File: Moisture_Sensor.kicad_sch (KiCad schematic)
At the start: 17 parts, among them J1 UPDI, J2 OLED SSD1306 0.96in, J3 SOIL SENSOR v1.2, J5 BATTERY 3xAAA, Q1 DMG3415U, SW1 READ BUTTON, U1 ATtiny1614-SSNR, U2 TPS22917DBVR

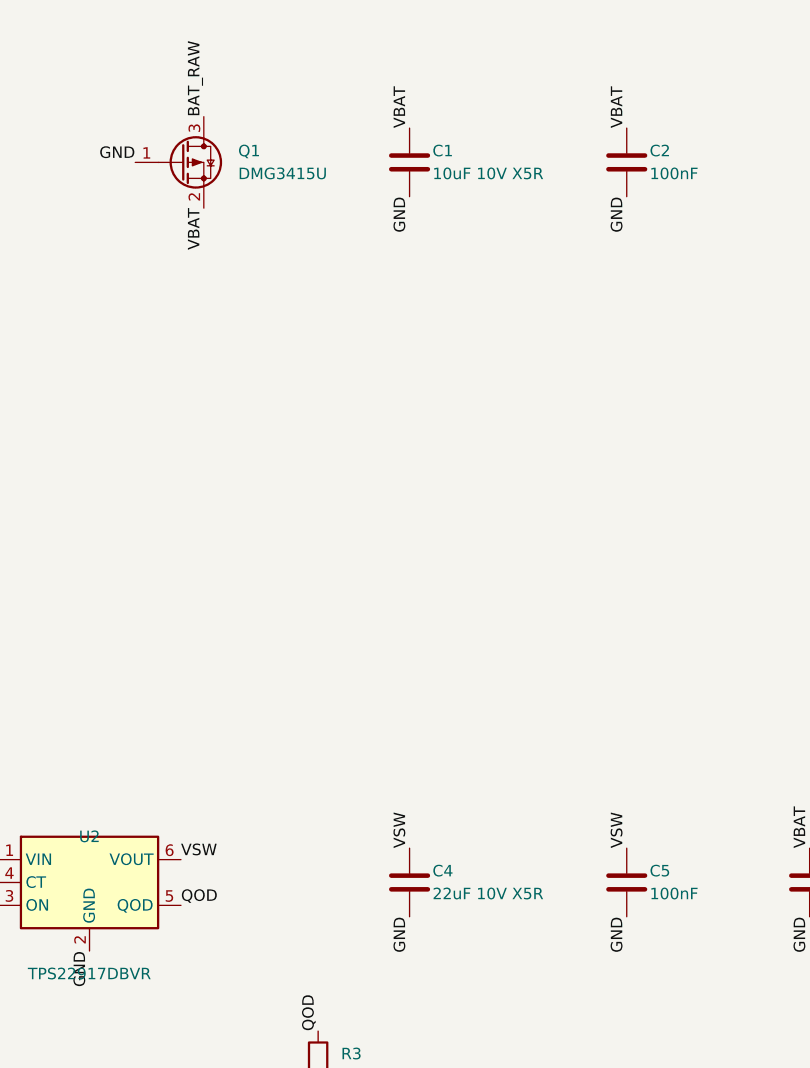
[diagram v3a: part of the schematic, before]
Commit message: JLCPCB BOM with LCSC part numbers; switch to JLC basic-library parts
- Add LCSC field to all placed parts (schematic + PCB)
- Passives -> JLC basic equivalents (C1/C4 now 25V), Q1 DMG3415U -> AO3401A (pin-compatible, basic)
- tools/gen_cpl.py now also writes fab/BOM_JLCPCB.csv

Co-authored-by: Copilot App <223556219+Copilot@users.noreply.github.com>
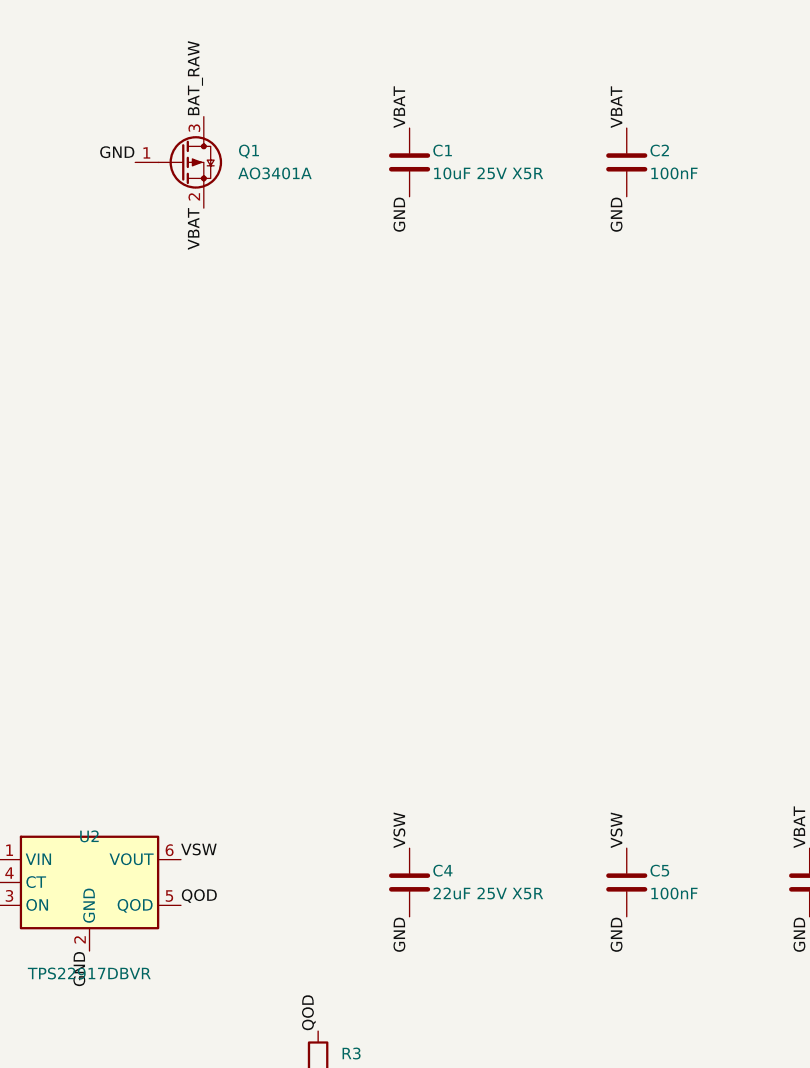
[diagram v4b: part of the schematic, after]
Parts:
- C1: value 10uF 10V X5R -> 10uF 25V X5R; LCSC (none) -> C15850; MPN CL21A106KPFNNNE -> CL21A106KAYNNNE
- C2, C5, C6: LCSC (none) -> C14663; MPN CL10B104KB8NNNC -> CC0603KRX7R9BB104; Manufacturer Samsung -> Yageo
- C3: LCSC (none) -> C1588
- C4: value 22uF 10V X5R -> 22uF 25V X5R; LCSC (none) -> C45783; MPN CL21A226MPQNNNE -> CL21A226MAQNNNE
- J5: LCSC (none) -> C131337
- Q1: value DMG3415U -> AO3401A; LCSC (none) -> C15127; MPN DMG3415U-7 -> AO3401A; Manufacturer Diodes Inc -> Alpha & Omega
- R1, R2: LCSC (none) -> C25804; MPN RC0603FR-0710KL -> 0603WAF1002T5E; Manufacturer Yageo -> UNI-ROYAL
- R3: LCSC (none) -> C21189; MPN RC0603JR-070RL -> 0603WAF0000T5E; Manufacturer Yageo -> UNI-ROYAL
- U1: LCSC (none) -> C481364
- U2: LCSC (none) -> C2681320
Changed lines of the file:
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@@
 	(title_block
 		(title "Soil Moisture Meter")
-		(date "2026-10-26")
+		(date "2026-10-27")
 		(rev "A")
 		(comment 1 "2xAAA, ATtiny1614, TPS22917 load switch, SSD1306 OLED, STEMMA soil sensor")
@@
 			)
 		)
+		(property "LCSC" "C131337"
+			(at 39.37 59.69 0)
+			(hide yes)
+			(effects
+				(font
+					(size 1.27 1.27)
+				)
+			)
+		)
 		(property "Note" "3xAAA holder (3.0-4.8V) with JST-PH leads, in case (pin1 = +)"
 			(at 39.37 59.69 0)
@@
 			)
 		)
-		(property "Value" "DMG3415U"
+		(property "Value" "AO3401A"
 			(at 86.36 60.96 0)
 			(effects
@@
 			)
 		)
-		(property "MPN" "DMG3415U-7"
+		(property "MPN" "AO3401A"
 			(at 80.01 59.69 0)
 			(hide yes)
@@
 			)
 		)
-		(property "Manufacturer" "Diodes Inc"
+		(property "Manufacturer" "Alpha & Omega"
+			(at 80.01 59.69 0)
+			(hide yes)
+			(effects
+				(font
+					(size 1.27 1.27)
+				)
+			)
+		)
+		(property "LCSC" "C15127"
 			(at 80.01 59.69 0)
 			(hide yes)
@@
 			)
 		)
-		(property "Value" "10uF 10V X5R"
+		(property "Value" "10uF 25V X5R"
 			(at 107.95 60.96 0)
 			(effects
@@
 			)
 		)
-		(property "MPN" "CL21A106KPFNNNE"
+		(property "MPN" "CL21A106KAYNNNE"
 			(at 105.41 59.69 0)
 			(hide yes)
@@
 		)
 		(property "Manufacturer" "Samsung"
+			(at 105.41 59.69 0)
+			(hide yes)
+			(effects
+				(font
+					(size 1.27 1.27)
+				)
+			)
+		)
+		(property "LCSC" "C15850"
 			(at 105.41 59.69 0)
 			(hide yes)
@@
 			)
 		)
-		(property "MPN" "CL10B104KB8NNNC"
+		(property "MPN" "CC0603KRX7R9BB104"
 			(at 129.54 59.69 0)
 			(hide yes)
@@
 			)
 		)
-		(property "Manufacturer" "Samsung"
+		(property "Manufacturer" "Yageo"
+			(at 129.54 59.69 0)
+			(hide yes)
+			(effects
+				(font
+					(size 1.27 1.27)
+				)
+			)
+		)
+		(property "LCSC" "C14663"
 			(at 129.54 59.69 0)
 			(hide yes)
@@
 			)
 		)
+		(property "LCSC" "C481364"
+			(at 199.39 129.54 0)
+			(hide yes)
+			(effects
+				(font
+					(size 1.27 1.27)
+				)
+			)
+		)
 		(pin "1"
 		)
@@
 			)
 		)
+		(property "LCSC" "C2681320"
+			(at 69.85 139.7 0)
+			(hide yes)
+			(effects
+				(font
+					(size 1.27 1.27)
+				)
+			)
+		)
 		(pin "1"
 		)
@@
 			)
 		)
-		(property "MPN" "RC0603JR-070RL"
+		(property "MPN" "0603WAF0000T5E"
 			(at 95.25 160.02 0)
 			(hide yes)
@@
 			)
 		)
-		(property "Manufacturer" "Yageo"
+		(property "Manufacturer" "UNI-ROYAL"
+			(at 95.25 160.02 0)
+			(hide yes)
+			(effects
+				(font
+					(size 1.27 1.27)
+				)
+			)
+		)
+		(property "LCSC" "C21189"
 			(at 95.25 160.02 0)
 			(hide yes)
@@
 			)
 		)
+		(property "LCSC" "C1588"
+			(at 39.37 165.1 0)
+			(hide yes)
+			(effects
+				(font
+					(size 1.27 1.27)
+				)
+			)
+		)
 		(property "Note" "Load switch slew-rate"
 			(at 39.37 165.1 0)
@@
 			)
 		)
-		(property "Value" "22uF 10V X5R"
+		(property "Value" "22uF 25V X5R"
 			(at 107.95 140.97 0)
 			(effects
@@
 			)
 		)
-		(property "MPN" "CL21A226MPQNNNE"
+		(property "MPN" "CL21A226MAQNNNE"
 			(at 105.41 139.7 0)
 			(hide yes)
@@
 		)
 		(property "Manufacturer" "Samsung"
+			(at 105.41 139.7 0)
+			(hide yes)
+			(effects
+				(font
+					(size 1.27 1.27)
+				)
+			)
+		)
+		(property "LCSC" "C45783"
 			(at 105.41 139.7 0)
 			(hide yes)
@@
 			)
 		)
-		(property "MPN" "CL10B104KB8NNNC"
+		(property "MPN" "CC0603KRX7R9BB104"
 			(at 129.54 139.7 0)
 			(hide yes)
@@
 			)
 		)
-		(property "Manufacturer" "Samsung"
+		(property "Manufacturer" "Yageo"
+			(at 129.54 139.7 0)
+			(hide yes)
+			(effects
+				(font
+					(size 1.27 1.27)
+				)
+			)
+		)
+		(property "LCSC" "C14663"
 			(at 129.54 139.7 0)
 			(hide yes)
@@
 			)
 		)
-		(property "MPN" "CL10B104KB8NNNC"
+		(property "MPN" "CC0603KRX7R9BB104"
 			(at 149.86 139.7 0)
 			(hide yes)
@@
 			)
 		)
-		(property "Manufacturer" "Samsung"
+		(property "Manufacturer" "Yageo"
+			(at 149.86 139.7 0)
+			(hide yes)
+			(effects
+				(font
+					(size 1.27 1.27)
+				)
+			)
+		)
+		(property "LCSC" "C14663"
 			(at 149.86 139.7 0)
 			(hide yes)
@@
 			)
 		)
-		(property "MPN" "RC0603FR-0710KL"
+		(property "MPN" "0603WAF1002T5E"
 			(at 270.51 59.69 0)
 			(hide yes)
@@
 			)
 		)
-		(property "Manufacturer" "Yageo"
+		(property "Manufacturer" "UNI-ROYAL"
+			(at 270.51 59.69 0)
+			(hide yes)
+			(effects
+				(font
+					(size 1.27 1.27)
+				)
+			)
+		)
+		(property "LCSC" "C25804"
 			(at 270.51 59.69 0)
 			(hide yes)
@@
 			)
 		)
-		(property "MPN" "RC0603FR-0710KL"
+		(property "MPN" "0603WAF1002T5E"
 			(at 284.48 59.69 0)
 			(hide yes)
@@
 			)
 		)
-		(property "Manufacturer" "Yageo"
+		(property "Manufacturer" "UNI-ROYAL"
 			(at 284.48 59.69 0)
 			(hide yes)
+			(effects
+				(font
+					(size 1.27 1.27)
+				)
+			)
+		)
+		(property "LCSC" "C25804"
+			(at 284.48 59.69 0)
+			(hide yes)

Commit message: Reroute PCB for 0.2 mm min track / 0.5 mm edge clearance; battery leads soldered to J5 pads
- J5 JST-PH replaced by 2x 2.54 mm TH wire pads (B+/B- silk), removed from JLC BOM/CPL
- gen_pcb: inset router outline for edge clearance, router clearance margin, widen necked tracks,
  solid GND connection on wire pads, preserve back-silk credit text
- DRC 0 violations / 0 unconnected with schematic parity; enclosure re-checked (0 interferences)

Co-authored-by: Copilot App <223556219+Copilot@users.noreply.github.com>
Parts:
- J5: footprint Connector_JST:JST_PH_B2B-PH-K_1x02_P2.00mm_Vertical -> Connector_PinHeader_2.54mm:PinHeader_1x02_P2.54mm_Vertical; LCSC C131337 -> (none); MPN B2B-PH-K-S(LF)(SN) -> 3xAAA holder leads soldered to pads; Manufacturer JST -> -; Note 3xAAA holder (3.0-4.8V) with JST-PH leads, in case (pin1 = 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 -> 3xAAA holder (3.0-4.8V) in case; pin1 = +, pin2 = -
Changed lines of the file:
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@@
 			)
 		)
-		(property "Footprint" "Connector_JST:JST_PH_B2B-PH-K_1x02_P2.00mm_Vertical"
+		(property "Footprint" "Connector_PinHeader_2.54mm:PinHeader_1x02_P2.54mm_Vertical"
 			(at 39.37 59.69 0)
 			(hide yes)
@@
 			)
 		)
-		(property "MPN" "B2B-PH-K-S(LF)(SN)"
+		(property "MPN" "3xAAA holder leads soldered to pads"
 			(at 39.37 59.69 0)
 			(hide yes)
@@
 			)
 		)
-		(property "Manufacturer" "JST"
+		(property "Manufacturer" "-"
 			(at 39.37 59.69 0)
 			(hide yes)
@@
 			)
 		)
-		(property "LCSC" "C131337"
+		(property "Note" "3xAAA holder (3.0-4.8V) in case; pin1 = +, pin2 = -"
 			(at 39.37 59.69 0)
 			(hide yes)
-			(effects
-				(font
-					(size 1.27 1.27)
-				)
-			)
-		)
-		(property "Note" "3xAAA holder (3.0-4.8V) with JST-PH leads, in case (pin1 = +)"
-			(at 39.37 59.69 0)
-			(hide yes)
